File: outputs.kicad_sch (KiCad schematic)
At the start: 12 parts, among them Q1 BT136-600, Q2 BT136-600, Q3 MOC3032M, Q4 MOC3032M

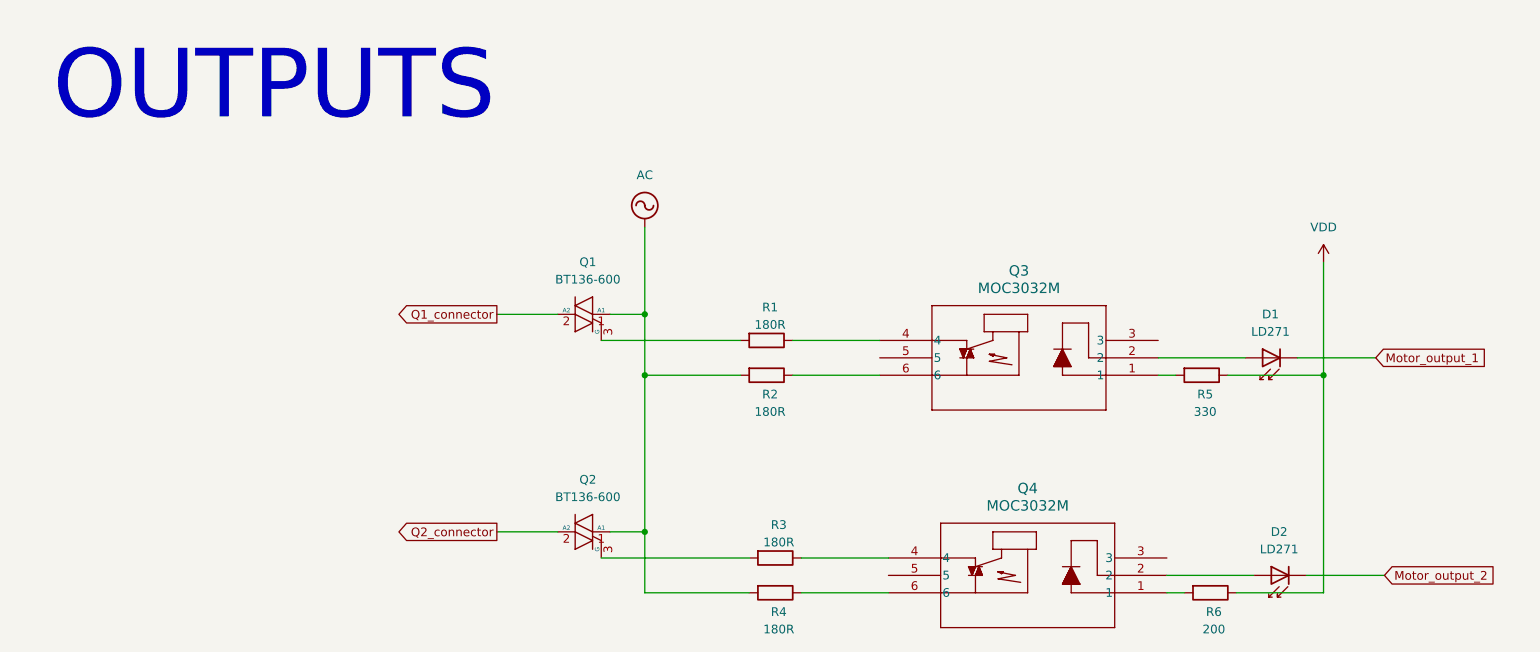
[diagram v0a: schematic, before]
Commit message: Dodanie footprintów
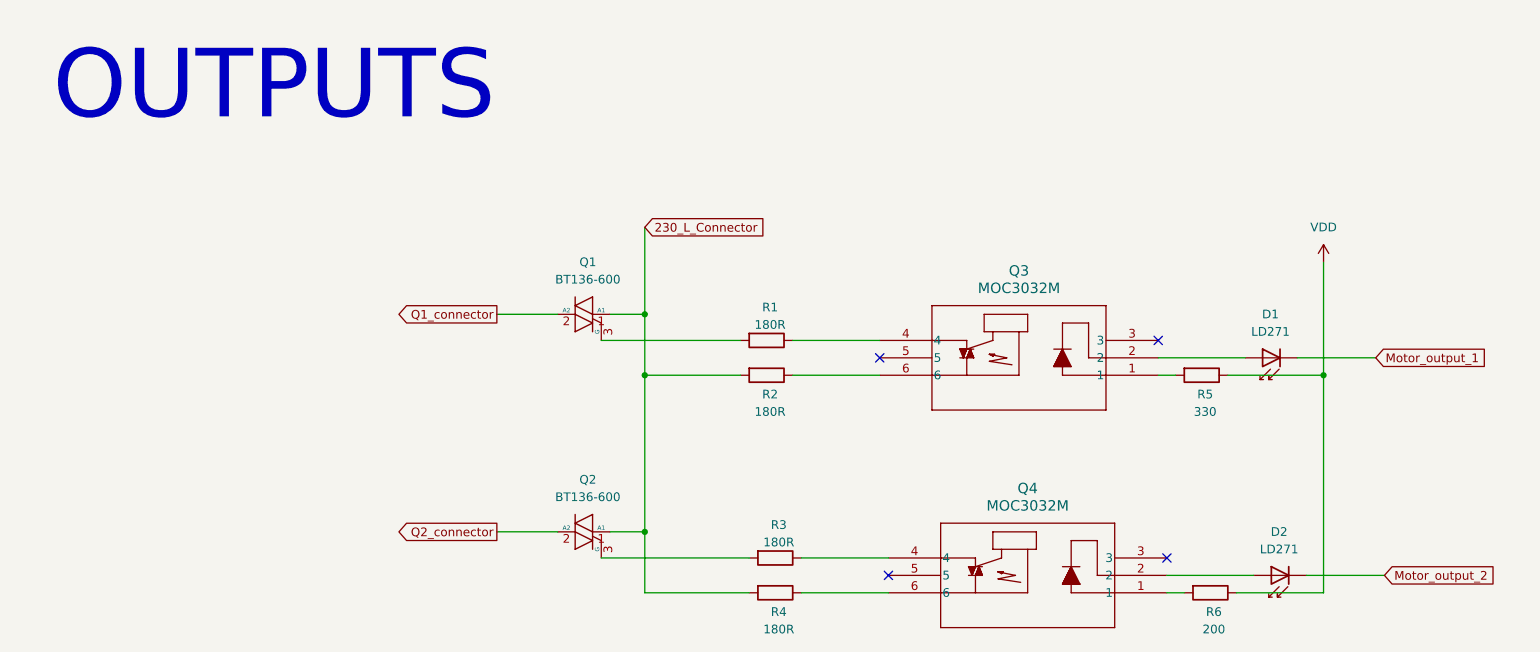
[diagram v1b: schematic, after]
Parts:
- Q3, Q4: footprint PDIP6-646BX_ONS -> Package_DIP:DIP-6_W7.62mm
- R1, R2, R3, R4, R5, R6: footprint (none) -> Resistor_SMD:R_0201_0603Metric
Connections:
- net AC renamed 230_L_Connector
- no-connect marks 0 -> 4
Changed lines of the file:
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@@
 		(color 0 0 0 0)
+	)
+	(no_connect
+		(at 189.23 97.79)
+	)
+	(no_connect
+		(at 147.32 68.58)
+	)
+	(no_connect
+		(at 187.96 66.04)
+	)
+	(no_connect
+		(at 148.59 100.33)
 	)
 	(wire
@@
 		)
 	)
+	(global_label "230_L_Connector"
+		(shape input)
+		(at 113.03 49.53 0)
+		(fields_autoplaced yes)
+		(effects
+			(font
+				(size 1.27 1.27)
+			)
+			(justify left)
+		)
+		(property "Intersheetrefs" "${INTERSHEET_REFS}"
+			(at 132.1621 49.53 0)
+			(effects
+				(font
+					(size 1.27 1.27)
+				)
+				(justify left)
+				(hide yes)
+			)
+		)
+	)
 	(symbol
 		(lib_id "Triac_Thyristor:BT136-600")
@@
 			)
 		)
-		(property "Footprint" ""
+		(property "Footprint" "Resistor_SMD:R_0201_0603Metric"
 			(at 194.31 69.342 90)
 			(effects
@@
 			)
 		)
-		(property "Footprint" ""
+		(property "Footprint" "Resistor_SMD:R_0201_0603Metric"
 			(at 130.81 69.342 90)
 			(effects
@@
 			)
 		)
-		(property "Footprint" "PDIP6-646BX_ONS"
+		(property "Footprint" "Package_DIP:DIP-6_W7.62mm"
 			(at 187.96 71.12 0)
 			(effects
@@
 			)
 		)
-		(property "Footprint" ""
+		(property "Footprint" "Resistor_SMD:R_0201_0603Metric"
 			(at 195.58 101.092 90)
 			(effects
@@
 			)
 		)
-		(property "Footprint" ""
+		(property "Footprint" "Resistor_SMD:R_0201_0603Metric"
 			(at 130.81 64.262 90)
 			(effects
@@
 	)
 	(symbol
-		(lib_id "power:AC")
-		(at 113.03 49.53 0)
-		(unit 1)
-		(exclude_from_sim no)
-		(in_bom yes)
-		(on_board yes)
-		(dnp no)
-		(fields_autoplaced yes)
-		(property "Reference" "#PWR07"
-			(at 113.03 52.07 0)
-			(effects
-				(font
-					(size 1.27 1.27)
-				)
-				(hide yes)
-			)
-		)
-		(property "Value" "AC"
-			(at 113.03 41.91 0)
-			(effects
-				(font
-					(size 1.27 1.27)
-				)
-			)
-		)
-		(property "Footprint" ""
-			(at 113.03 49.53 0)
-			(effects
-				(font
-					(size 1.27 1.27)
-				)
-				(hide yes)
-			)
-		)
-		(property "Datasheet" ""
-			(at 113.03 49.53 0)
-			(effects
-				(font
-					(size 1.27 1.27)
-				)
-				(hide yes)
-			)
-		)
-		(property "Description" "Power symbol creates a global label with name \"AC\""
-			(at 113.03 49.53 0)
-			(effects
-				(font
-					(size 1.27 1.27)
-				)
-				(hide yes)
-			)
-		)
-		(pin "1"
-		)
-		(instances
-			(project ""
-				(path "/e63e39d7-6ac0-4ffd-8aa3-1841a4541b55/c3498625-d7cb-47e3-b571-b13207fdad6e"
-					(reference "#PWR07")
-					(unit 1)
-				)
-			)
-		)
-	)
-	(symbol
 		(lib_id "LED:LD271")
 		(at 203.2 68.58 180)
@@
 			)
 		)
-		(property "Footprint" "PDIP6-646BX_ONS"
+		(property "Footprint" "Package_DIP:DIP-6_W7.62mm"
 			(at 189.23 102.87 0)
 			(effects
@@
 			)
 		)
-		(property "Footprint" ""
+		(property "Footprint" "Resistor_SMD:R_0201_0603Metric"
 			(at 132.08 96.012 90)
 			(effects
@@
 		(dnp no)
 		(fields_autoplaced yes)
-		(property "Reference" "#PWR08"
+		(property "Reference" "#PWR013"
 			(at 212.09 58.42 0)
 			(effects
@@
 			(project ""
 				(path "/e63e39d7-6ac0-4ffd-8aa3-1841a4541b55/c3498625-d7cb-47e3-b571-b13207fdad6e"
-					(reference "#PWR08")
+					(reference "#PWR013")
 					(unit 1)
 				)
@@
 			)
 		)
-		(property "Footprint" ""
+		(property "Footprint" "Resistor_SMD:R_0201_0603Metric"
 			(at 132.08 101.092 90)
 			(effects

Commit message: początkowe rozłożenie na PCB
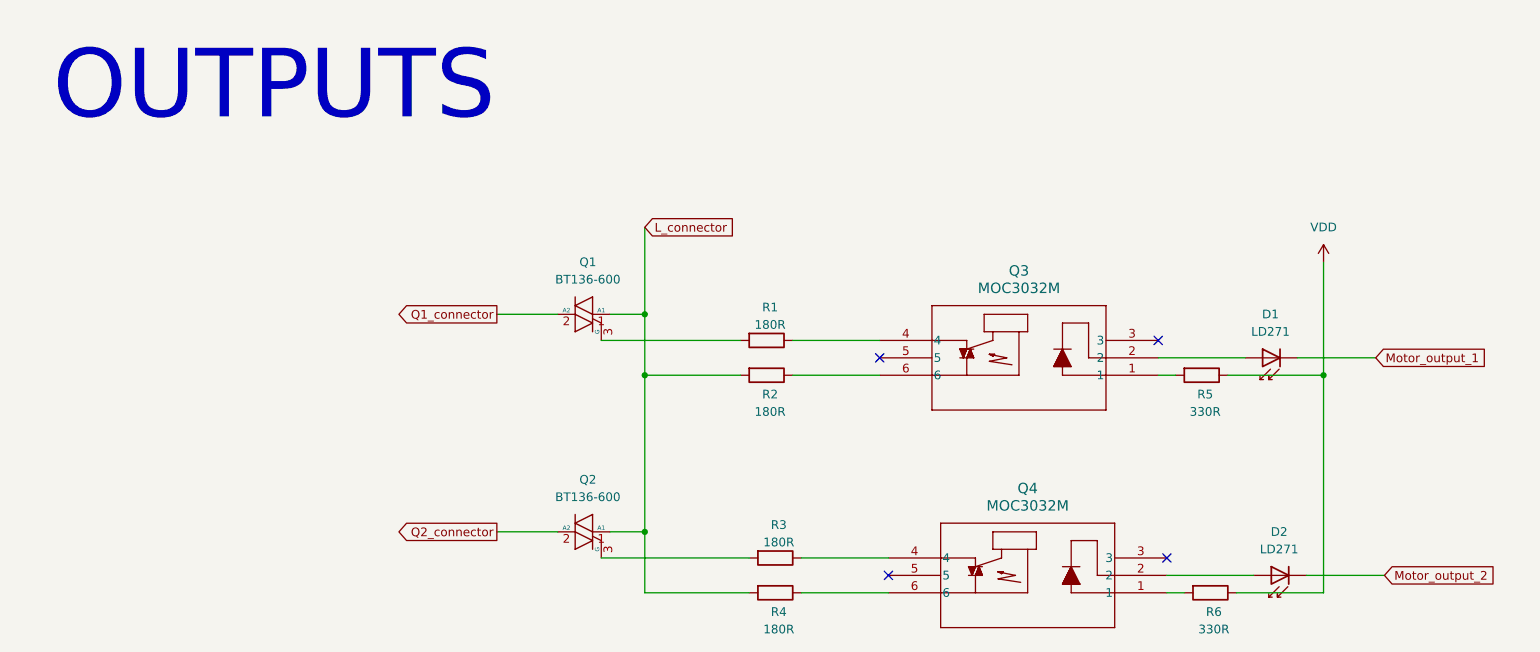
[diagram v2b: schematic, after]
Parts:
- R5: value 330 -> 330R
- R6: value 200 -> 330R
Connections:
- net 230_L_Connector renamed L_connector
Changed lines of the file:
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@@
 		)
 	)
-	(global_label "230_L_Connector"
+	(global_label "L_connector"
 		(shape input)
 		(at 113.03 49.53 0)
@@
 		)
 		(property "Intersheetrefs" "${INTERSHEET_REFS}"
-			(at 132.1621 49.53 0)
+			(at 127.3846 49.53 0)
 			(effects
 				(font
@@
 			)
 		)
-		(property "Value" "330"
+		(property "Value" "330R"
 			(at 194.818 76.454 90)
 			(effects
@@
 			)
 		)
-		(property "Value" "200"
+		(property "Value" "330R"
 			(at 196.088 108.204 90)
 			(effects
